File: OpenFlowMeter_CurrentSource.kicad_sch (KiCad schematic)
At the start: 21 parts, among them J1 Screw_Terminal_01x02, Q1 BC856, U1 LT1492

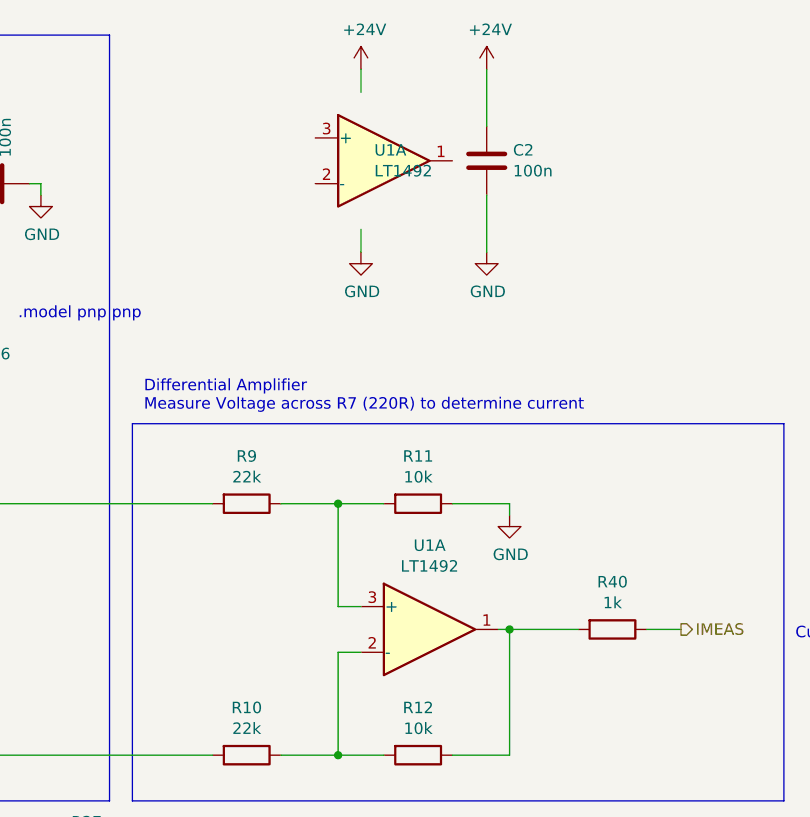
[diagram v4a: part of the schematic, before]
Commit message: small update
some very small changes from my approach of simulating eveything using KiCAD
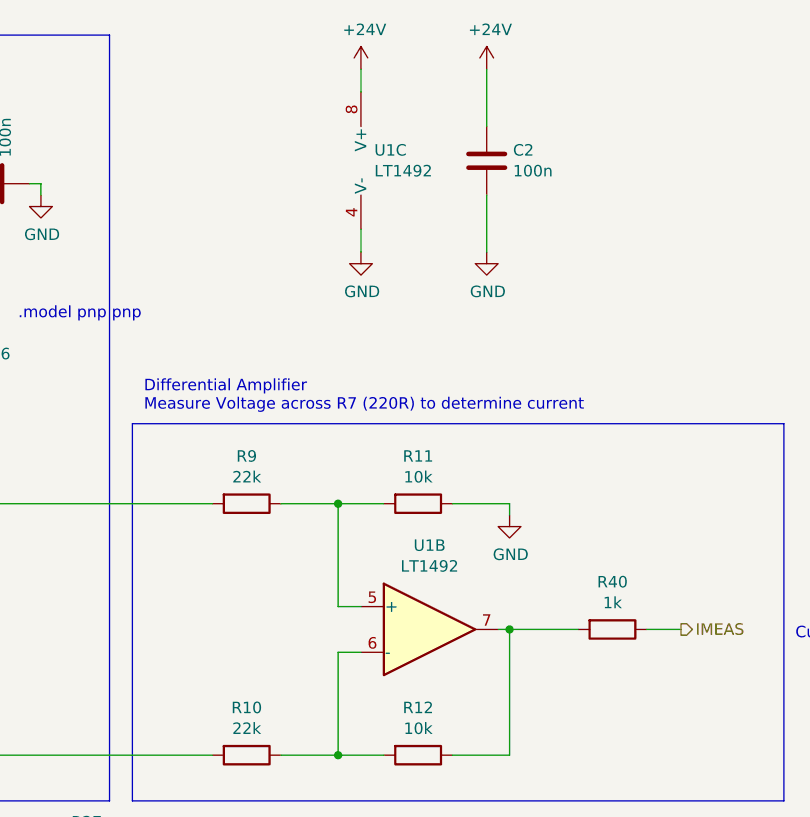
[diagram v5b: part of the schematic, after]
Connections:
- net +24V: now also U1.8 (V+)
- net GND: now also U1.4 (V-)
- net at R12.1, R40.2: now also U1.7; no longer U1.1
- net at R10.1, R12.2: now also U1.6 (-); no longer U1.2 (-)
- net at R11.2, R9.1: now also U1.5 (+); no longer U1.3 (+)
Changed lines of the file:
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@@
     (effects (font (size 1.27 1.27)) (justify left))
   )
-  (symbol (lib_id "Amplifier_Operational:LT1492") (at 90.17 83.82 0) (mirror x)
+  (symbol (lib_id "Amplifier_Operational:LT1492") (at 90.17 83.82 0) (mirror x) (unit 1)
     (in_bom yes) (on_board yes)
     (property "Reference" "U1" (id 0) (at 90.17 93.1418 0))
@@
     (pin "3")
   )
-  (symbol (lib_id "Amplifier_Operational:LT1492") (at 172.72 115.57 0)
+  (symbol (lib_id "Amplifier_Operational:LT1492") (at 172.72 115.57 0) (unit 2)
     (in_bom yes) (on_board yes)
     (property "Reference" "U1" (id 0) (at 172.72 106.2482 0))
@@
     (pin "7")
   )
-  (symbol (lib_id "Amplifier_Operational:LT1492") (at 167.64 63.5 0)
+  (symbol (lib_id "Amplifier_Operational:LT1492") (at 167.64 63.5 0) (unit 3)
     (in_bom yes) (on_board yes)
     (property "Reference" "U1" (id 0) (at 166.5732 62.3316 0)
@@
     (pin "8")
   )
-  (symbol (lib_id "Device:R") (at 50.8 81.28 270)
+  (symbol (lib_id "Device:R") (at 50.8 81.28 270) (unit 1)
     (in_bom yes) (on_board yes)
     (property "Reference" "R1" (id 0) (at 50.8 76.0222 90))
@@
     (pin "2")
   )
-  (symbol (lib_id "Device:R") (at 102.87 129.54 270)
+  (symbol (lib_id "Device:R") (at 102.87 129.54 270) (unit 1)
     (in_bom yes) (on_board yes)
     (property "Reference" "R4" (id 0) (at 102.87 124.2822 90))
@@
     (pin "2")
   )
-  (symbol (lib_id "Device:R") (at 118.11 72.39 0)
+  (symbol (lib_id "Device:R") (at 118.11 72.39 0) (unit 1)
     (in_bom yes) (on_board yes)
     (property "Reference" "R6" (id 0) (at 119.888 71.2216 0)
@@
     (pin "2")
   )
-  (symbol (lib_id "Device:R") (at 104.14 83.82 270)
+  (symbol (lib_id "Device:R") (at 104.14 83.82 270) (unit 1)
     (in_bom yes) (on_board yes)
     (property "Reference" "R5" (id 0) (at 104.14 78.5622 90))
@@
     (pin "2")
   )
-  (symbol (lib_id "Device:R") (at 118.11 115.57 0)
+  (symbol (lib_id "Device:R") (at 118.11 115.57 0) (unit 1)
     (in_bom yes) (on_board yes)
     (property "Reference" "R7" (id 0) (at 119.888 114.4016 0)
@@
     (pin "2")
   )
-  (symbol (lib_id "Device:R") (at 102.87 101.6 270)
+  (symbol (lib_id "Device:R") (at 102.87 101.6 270) (unit 1)
     (in_bom yes) (on_board yes)
     (property "Reference" "R3" (id 0) (at 102.87 96.3422 90))
@@
     (pin "2")
   )
-  (symbol (lib_id "Device:R") (at 74.93 101.6 270)
+  (symbol (lib_id "Device:R") (at 74.93 101.6 270) (unit 1)
     (in_bom yes) (on_board yes)
     (property "Reference" "R2" (id 0) (at 74.93 96.3422 90))
@@
     (pin "2")
   )
-  (symbol (lib_id "power:GND") (at 68.58 105.41 0)
+  (symbol (lib_id "power:GND") (at 68.58 105.41 0) (unit 1)
     (in_bom yes) (on_board yes)
     (property "Reference" "#PWR02" (id 0) (at 68.58 111.76 0)
@@
     (pin "1")
   )
-  (symbol (lib_id "power:+24V") (at 118.11 64.77 0)
+  (symbol (lib_id "power:+24V") (at 118.11 64.77 0) (unit 1)
     (in_bom yes) (on_board yes)
     (property "Reference" "#PWR03" (id 0) (at 118.11 68.58 0)
@@
     (pin "1")
   )
-  (symbol (lib_id "power:+24V") (at 165.1 53.34 0)
+  (symbol (lib_id "power:+24V") (at 165.1 53.34 0) (unit 1)
     (in_bom yes) (on_board yes)
     (property "Reference" "#PWR05" (id 0) (at 165.1 57.15 0)
@@
     (pin "1")
   )
-  (symbol (lib_id "power:GND") (at 165.1 73.66 0)
+  (symbol (lib_id "power:GND") (at 165.1 73.66 0) (unit 1)
     (in_bom yes) (on_board yes)
     (property "Reference" "#PWR06" (id 0) (at 165.1 80.01 0)
@@
     (pin "1")
   )
-  (symbol (lib_id "Device:R") (at 152.4 101.6 270)
+  (symbol (lib_id "Device:R") (at 152.4 101.6 270) (unit 1)
     (in_bom yes) (on_board yes)
     (property "Reference" "R9" (id 0) (at 152.4 96.3422 90))
@@
     (pin "2")
   )
-  (symbol (lib_id "Device:R") (at 152.4 129.54 270)
+  (symbol (lib_id "Device:R") (at 152.4 129.54 270) (unit 1)
     (in_bom yes) (on_board yes)
     (property "Reference" "R10" (id 0) (at 152.4 124.2822 90))
@@
     (pin "2")
   )
-  (symbol (lib_id "Device:R") (at 171.45 101.6 270)
+  (symbol (lib_id "Device:R") (at 171.45 101.6 270) (unit 1)
     (in_bom yes) (on_board yes)
     (property "Reference" "R11" (id 0) (at 171.45 96.3422 90))
@@
     (pin "2")
   )
-  (symbol (lib_id "Device:R") (at 171.45 129.54 270)
+  (symbol (lib_id "Device:R") (at 171.45 129.54 270) (unit 1)
     (in_bom yes) (on_board yes)
     (property "Reference" "R12" (id 0) (at 171.45 124.2822 90))
@@
     (pin "2")
   )
-  (symbol (lib_id "power:GND") (at 181.61 102.87 0)
+  (symbol (lib_id "power:GND") (at 181.61 102.87 0) (unit 1)
     (in_bom yes) (on_board yes)
     (property "Reference" "#PWR07" (id 0) (at 181.61 109.22 0)
@@
     (pin "1")
   )
-  (symbol (lib_id "power:GND") (at 118.11 168.91 0)
+  (symbol (lib_id "power:GND") (at 118.11 168.91 0) (unit 1)
     (in_bom yes) (on_board yes)
     (property "Reference" "#PWR04" (id 0) (at 118.11 175.26 0)
@@
     (pin "1")
   )
-  (symbol (lib_id "Transistor_BJT:BC856") (at 115.57 83.82 0) (mirror x)
+  (symbol (lib_id "Transistor_BJT:BC856") (at 115.57 83.82 0) (mirror x) (unit 1)
     (in_bom yes) (on_board yes)
     (property "Reference" "Q1" (id 0) (at 120.4214 82.6516 0)
@@
     (pin "3")
   )
-  (symbol (lib_id "Connector:Screw_Terminal_01x02") (at 135.89 154.94 0)
+  (symbol (lib_id "Connector:Screw_Terminal_01x02") (at 135.89 154.94 0) (unit 1)
     (in_bom yes) (on_board yes)
     (property "Reference" "J1" (id 0) (at 137.922 155.1432 0)
@@
     (pin "2")
   )
-  (symbol (lib_id "power:GND") (at 129.54 168.91 0)
+  (symbol (lib_id "power:GND") (at 129.54 168.91 0) (unit 1)
     (in_bom yes) (on_board yes)
     (property "Reference" "#PWR0110" (id 0) (at 129.54 175.26 0)
@@
     (pin "1")
   )
-  (symbol (lib_id "Device:R") (at 134.62 142.24 270)
+  (symbol (lib_id "Device:R") (at 134.62 142.24 270) (unit 1)
     (in_bom yes) (on_board yes)
     (property "Reference" "R27" (id 0) (at 134.62 136.9822 90))
@@
     (pin "2")
   )
-  (symbol (lib_id "Sensor_Temperature:PT100") (at 118.11 156.21 0)
+  (symbol (lib_id "Sensor_Temperature:PT100") (at 118.11 156.21 0) (unit 1)
     (in_bom yes) (on_board yes)
     (property "Reference" "TH1" (id 0) (at 120.5992 155.0416 0)
@@
     (pin "2")
   )
-  (symbol (lib_id "Device:C") (at 179.07 63.5 0)
+  (symbol (lib_id "Device:C") (at 179.07 63.5 0) (unit 1)
     (in_bom yes) (on_board yes)
     (property "Reference" "C2" (id 0) (at 181.991 62.3316 0)
@@
     (pin "2")
   )
-  (symbol (lib_id "Device:C") (at 124.46 66.04 90)
+  (symbol (lib_id "Device:C") (at 124.46 66.04 90) (unit 1)
     (in_bom yes) (on_board yes)
     (property "Reference" "C1" (id 0) (at 123.2916 63.119 0)
@@
     (pin "2")
   )
-  (symbol (lib_id "power:GND") (at 129.54 67.31 0)
+  (symbol (lib_id "power:GND") (at 129.54 67.31 0) (unit 1)
     (in_bom yes) (on_board yes)
     (property "Reference" "#PWR011" (id 0) (at 129.54 73.66 0)
@@
     (pin "1")
   )
-  (symbol (lib_id "power:GND") (at 179.07 73.66 0)
+  (symbol (lib_id "power:GND") (at 179.07 73.66 0) (unit 1)
     (in_bom yes) (on_board yes)
     (property "Reference" "#PWR013" (id 0) (at 179.07 80.01 0)
@@
     (pin "1")
   )
-  (symbol (lib_id "power:+24V") (at 179.07 53.34 0)
+  (symbol (lib_id "power:+24V") (at 179.07 53.34 0) (unit 1)
     (in_bom yes) (on_board yes)
     (property "Reference" "#PWR012" (id 0) (at 179.07 57.15 0)
@@
     (pin "1")
   )
-  (symbol (lib_id "Device:R") (at 193.04 115.57 270)
+  (symbol (lib_id "Device:R") (at 193.04 115.57 270) (unit 1)
     (in_bom yes) (on_board yes)
     (property "Reference" "R40" (id 0) (at 193.04 110.3122 90))

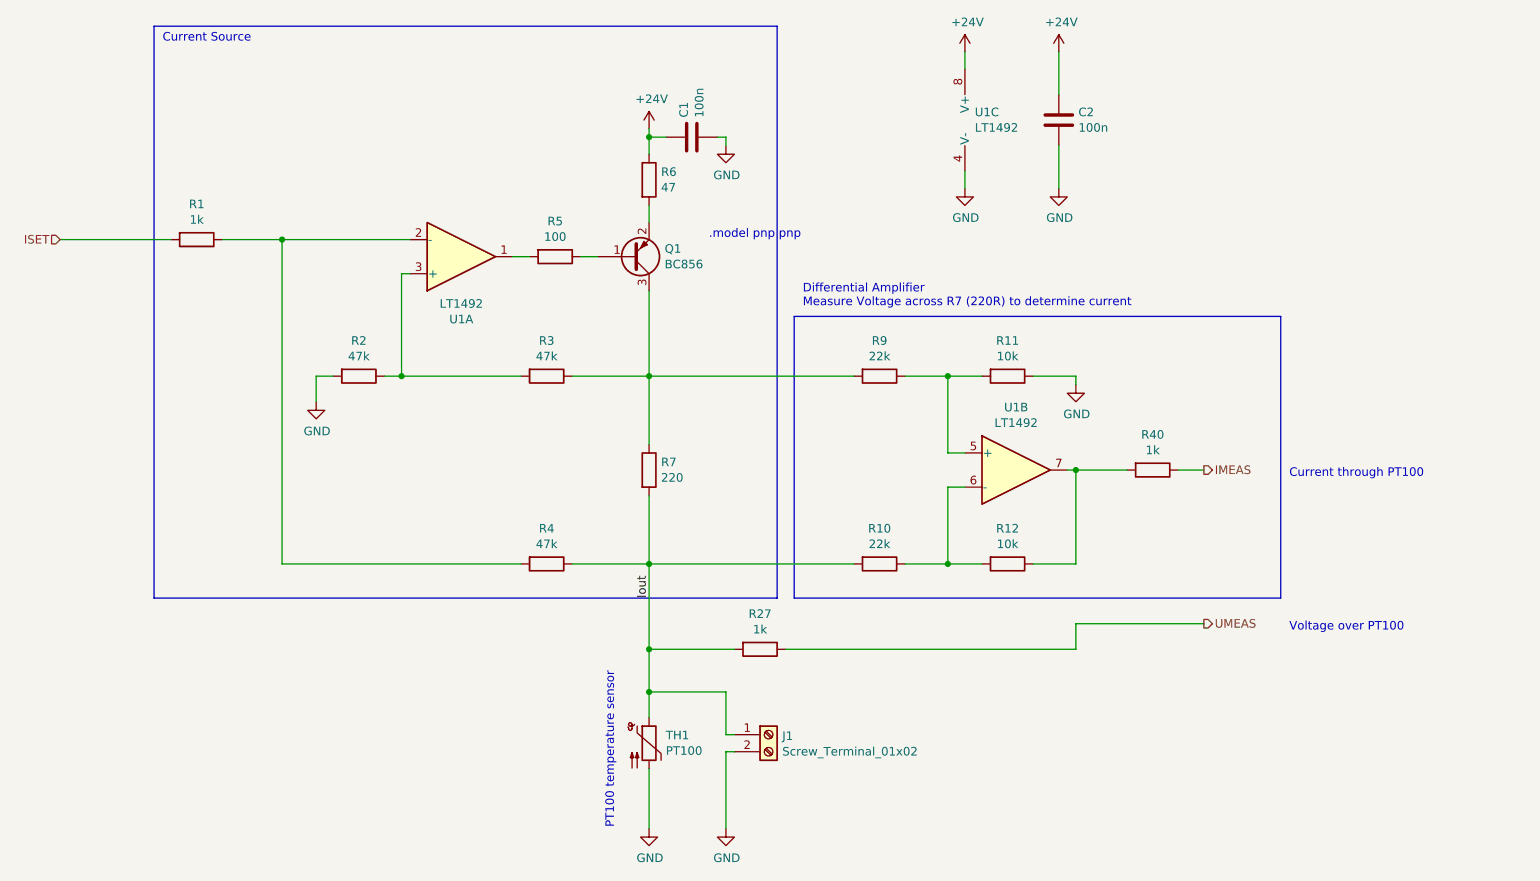
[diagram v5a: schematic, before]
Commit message: included values from simulation
added values to those components, which did not had one
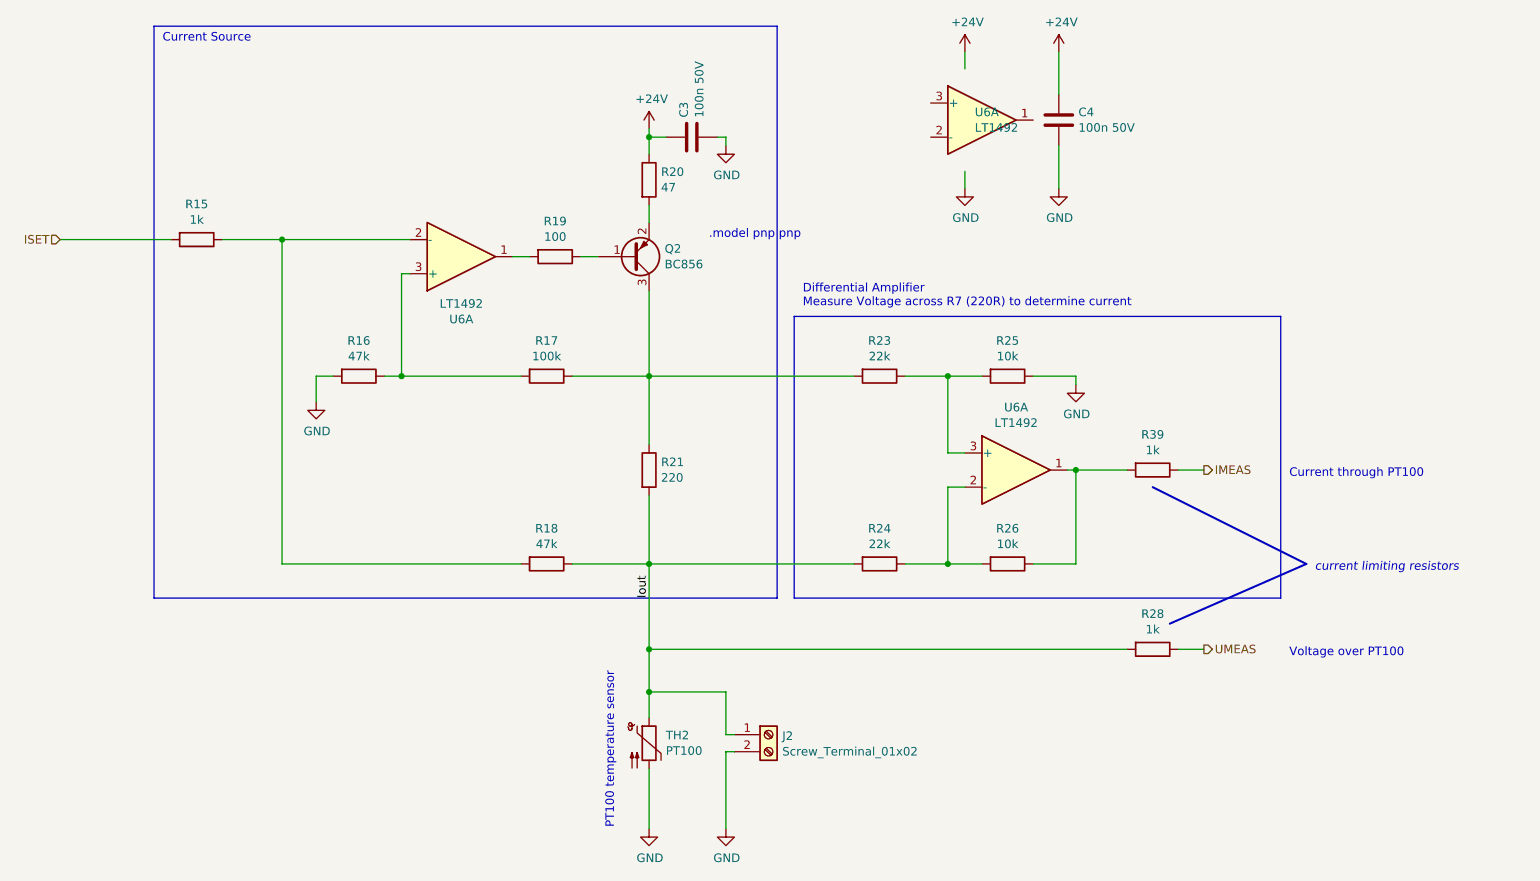
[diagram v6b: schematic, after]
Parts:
- C3: renamed from C1; value 100n -> 100n 50V
- C4: renamed from C2; value 100n -> 100n 50V
- R17: renamed from R3; value 47k -> 100k
- renumbered J1 to J2, Q1 to Q2, R1 to R15, R2 to R16, R4 to R18, R5 to R19, R6 to R20, R7 to R21, R9 to R23, R10 to R24, R11 to R25, R12 to R26, R27 to R28, R40 to R39, TH1 to TH2, U1 to U6
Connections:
- net +24V: no longer U6.8 (V+)
- net GND: no longer U6.4 (V-)
- net at R23.1, R25.2: now also U6.3 (+); no longer U6.5 (+)
- net at R24.1, R26.2: now also U6.2 (-); no longer U6.6 (-)
- net at R26.1, R39.2: now also U6.1; no longer U6.7
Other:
- note added: "current limiting resistors"
- moved on the sheet: R28
